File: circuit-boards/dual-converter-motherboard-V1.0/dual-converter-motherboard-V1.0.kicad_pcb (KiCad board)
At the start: 6 copper layers, 230 x 76 mm, 109 parts, among them J1 2601-1102, J10 Conn_02x03_Odd_Even, J11 Conn_01x06_Socket, J12 Conn_02x03_Odd_Even, J13 Conn_02x03_Odd_Even, J14 Conn_02x03_Odd_Even, J15 Conn_01x06_Socket, J16 Conn_01x07_Socket, J2 2601-1102, J3 S4B-XH-SM4-TB, J4 Conn_02x03_Odd_Even, J5 Conn_02x03_Odd_Even, J6 Conn_02x03_Odd_Even, J7 Conn_02x03_Odd_Even, J8 Conn_02x03_Odd_Even, J9 Conn_02x03_Odd_Even, Q1 SUM110P08-11L-E3, Q2 DMP45H4D9HK3-13, Q3 SIHB068N60EF-GE3, U4 UCC23313BDWYR, U5 TMCS1133C1A, U6 UCC23313BDWYR, U7 UCC23313BDWYR, U8 SC0915

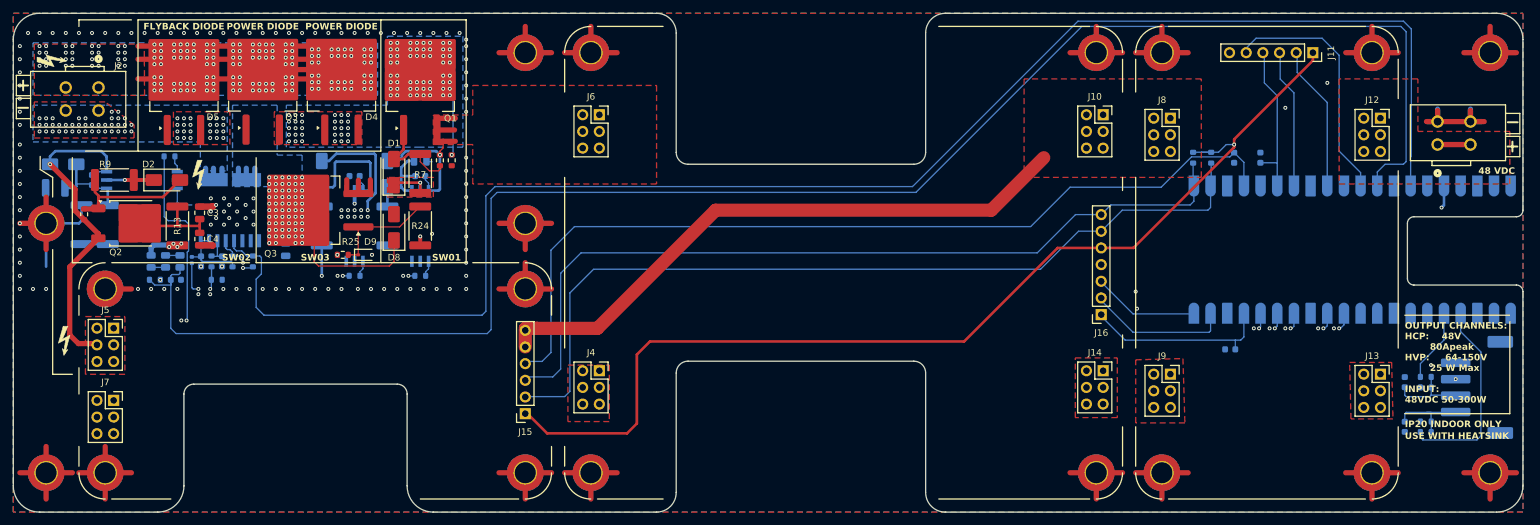
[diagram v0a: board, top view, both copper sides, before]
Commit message: final drc checks, silkscreen edits, added stitching vias to motherboard and pi filter
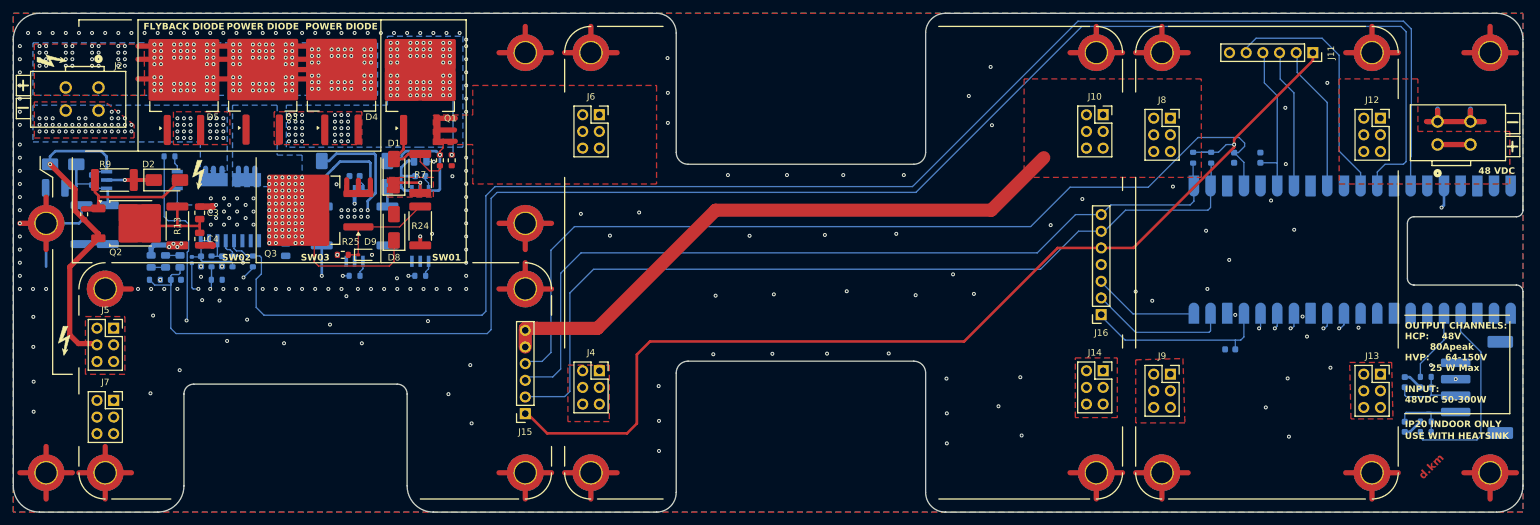
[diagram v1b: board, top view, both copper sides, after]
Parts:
- removed the REF** at (77.0, 78.0)
- removed the REF** at (59.0, 78.0)
- moved REF** 19.6 mm to (85.6, 42.4)
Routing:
- net +3.3V: track 346.2 -> 323.5 mm
- net GND: track 290.1 -> 297.2 mm, vias 145 -> 211
- net /BOOST_PGOOD: track 136.0 -> 141.4 mm
- net +48V: track 139.9 -> 137.2 mm
- net +18V: track 21.7 -> 20.3 mm
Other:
- board text added: "POWERCORE V3-EPL"
- board text added: "Reworked for EPL by Wire EDM Capstone"
- board text added: "d.km"
- board text added: "rev0 -- March 2026"
- board text removed: "POWERCORE V3 MOTHERBOARD RevH"
